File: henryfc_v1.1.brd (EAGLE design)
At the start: 36 x 36 mm, 69 parts, among them IC1 LM317DCYR, IC2 ICM-20602, IC3 AT7456E, IC4 STM32F722RET6TR, IC5 LM317DCYR, J2 10118192-0001LF, X1 SM07B-SRSS-TB, Y1 NX3225GA-27.000M-STD-CRG-1

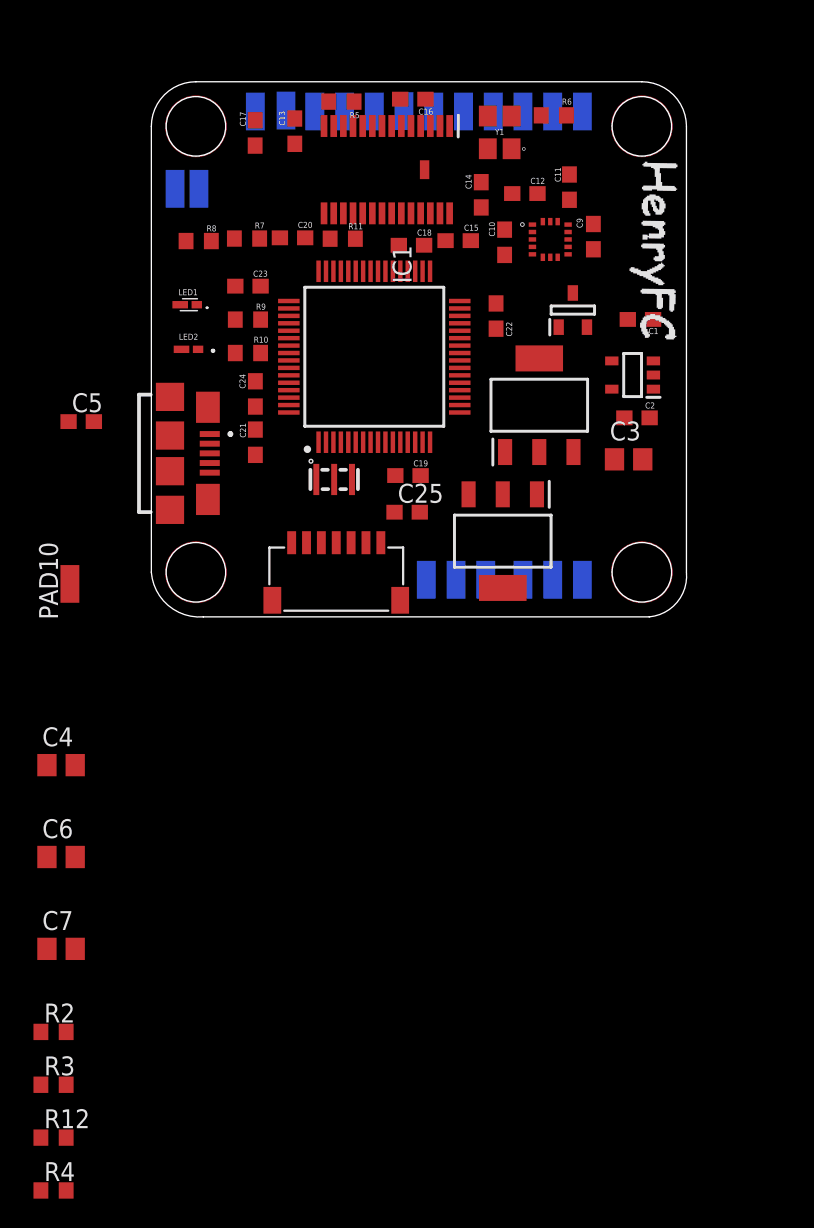
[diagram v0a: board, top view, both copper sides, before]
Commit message: edit bypass caps
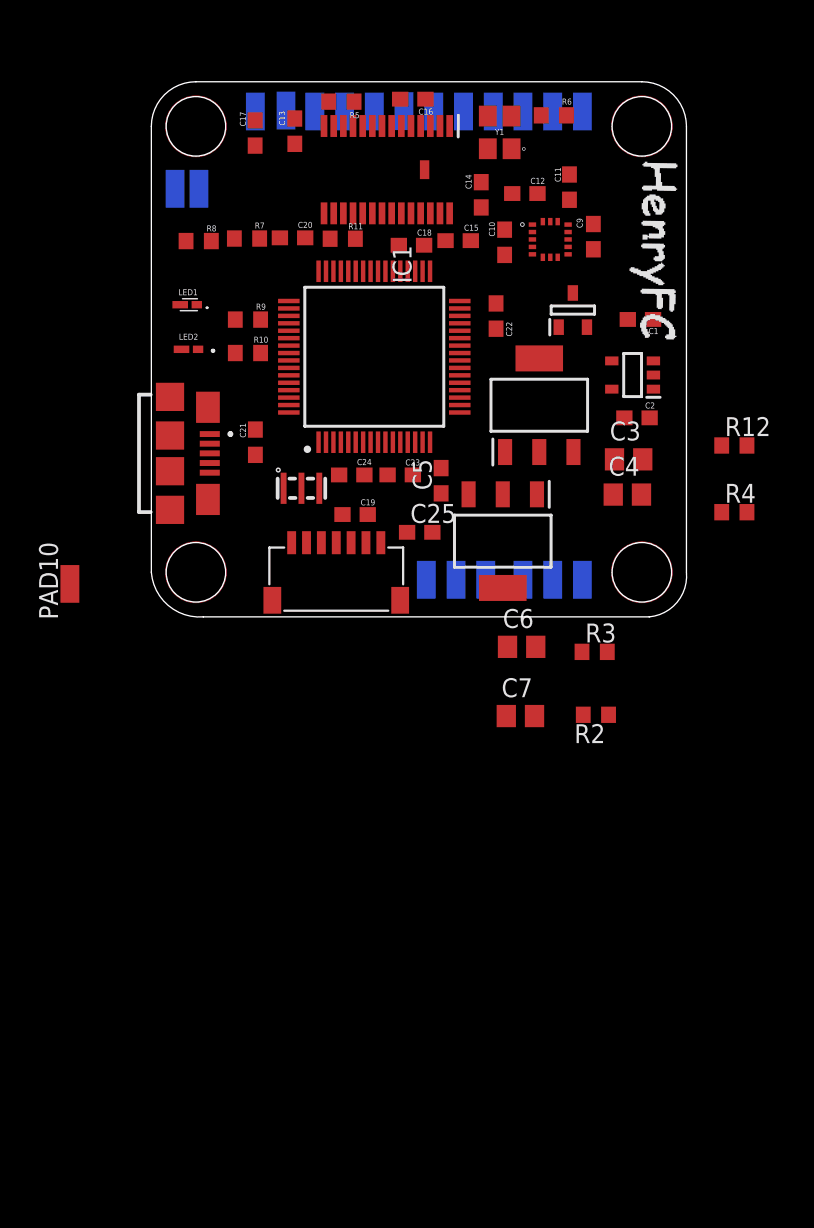
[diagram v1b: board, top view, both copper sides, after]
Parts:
- moved R12 65.3 mm to (40.7, 12.5)
- moved R4 64.7 mm to (40.7, 8.04)
- moved R3 46.6 mm to (31.3, -1.35)
- moved R2 42.3 mm to (31.4, -5.59), turned to 180 degrees
- moved C4 42.2 mm to (33.5, 9.23)
- moved C7 34.6 mm to (26.3, -5.67)
- moved C6 34.1 mm to (26.4, -1.02)
- moved C5 24.5 mm to (21.0, 10.2), turned to 90 degrees
- moved C23 16.3 mm to (18.2, 10.6)
- moved C24 8.47 mm to (15.0, 10.5), turned to 0 degrees
- moved C19 4.42 mm to (15.2, 7.88)
- moved R1 2.28 mm to (11.6, 9.65)
- moved C25 1.60 mm to (19.6, 6.69)

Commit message: update PCB layout
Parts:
- removed PAD10: BOOT, wirepad:SMD1,27-2,54
- added C26: 10uF, rcl:C0805
- added C8: 0.1uF, rcl:C0805
- moved R4 27.9 mm to (26.8, 32.2), turned to 90 degrees
- moved R12 22.6 mm to (29.5, 32.2)
- moved R6 21.7 mm to (7.73, 28.7), turned to 270 degrees
- moved R7 19.7 mm to (7.83, 6.71), turned to 270 degrees
- moved C21 18.6 mm to (24.2, 22.8), turned to 90 degrees
- moved C20 17.3 mm to (24.2, 15.4), turned to 270 degrees
- moved R8 16.8 mm to (8.34, 9.87), turned to 270 degrees
- moved Y1 15.4 mm to (9.53, 32.7)
- moved C19 14.8 mm to (24.2, 19.6), turned to 270 degrees
- moved C2 14.7 mm to (26.6, 27.0), turned to 180 degrees
- moved C11 14.5 mm to (30.1, 15.5), turned to 90 degrees
- moved C25 14.4 mm to (8.47, 15.9), turned to 90 degrees
- moved C10 14.1 mm to (27.5, 12.3), turned to 0 degrees
- moved R2 13.6 mm to (20.8, 2.88), turned to 0 degrees
- moved C7 13.5 mm to (23.0, 7.45), turned to 90 degrees
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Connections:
- net +5V: now also C26.2, C8.2; no longer PAD19.1, PAD20.1
- net 3.3V_REG: no longer PAD10.1
- net 5V_REG1: now also PAD19.1, PAD20.1
- net GND: now also C26.1, C8.1
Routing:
- net 3.3V_REG: track 0.00 -> 53.0 mm, vias 0 -> 1
- net 5V_REG1: track 0.00 -> 44.0 mm, vias 0 -> 1
- net VCC: track 0.00 -> 43.5 mm
- net 5V_USB: track 0.00 -> 34.0 mm, vias 0 -> 2
- net M3: track 0.00 -> 23.0 mm, vias 0 -> 2
- net +5V: track 0.00 -> 23.0 mm, vias 0 -> 1
- net M2: track 0.00 -> 23.0 mm, vias 0 -> 2
- net M1: track 0.00 -> 22.8 mm, vias 0 -> 2
- net M4: track 0.00 -> 22.8 mm, vias 0 -> 2
- net CURRENT_METER_ADC_PIN: track 0.00 -> 15.4 mm, vias 0 -> 2
- net VBAT_ADC_PIN: track 0.00 -> 14.5 mm
- net OSC_OUT: track 0.00 -> 11.7 mm
- net N$2: track 0.00 -> 11.6 mm
- net N$1: track 0.00 -> 11.1 mm
- net GYRO_1_CS_PIN: track 0.00 -> 10.5 mm
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
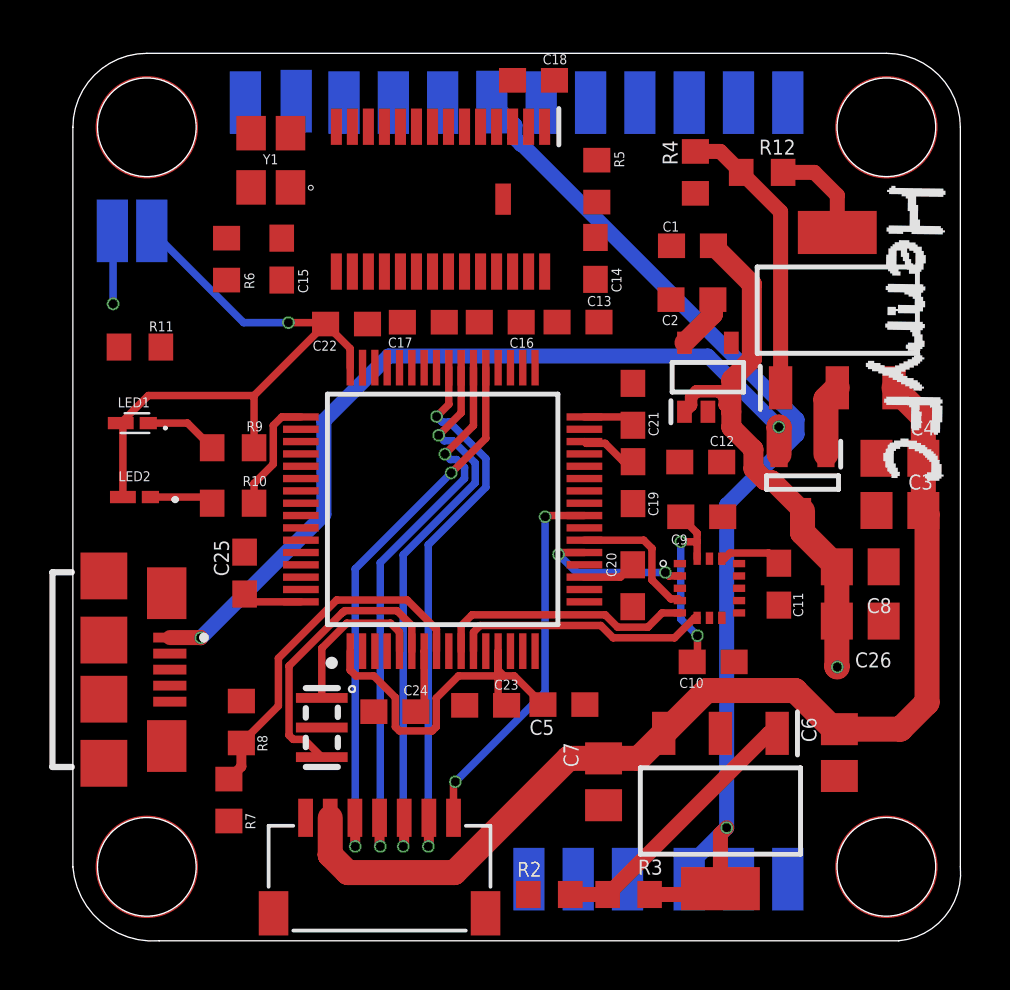
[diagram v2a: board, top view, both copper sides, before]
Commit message: update schematic
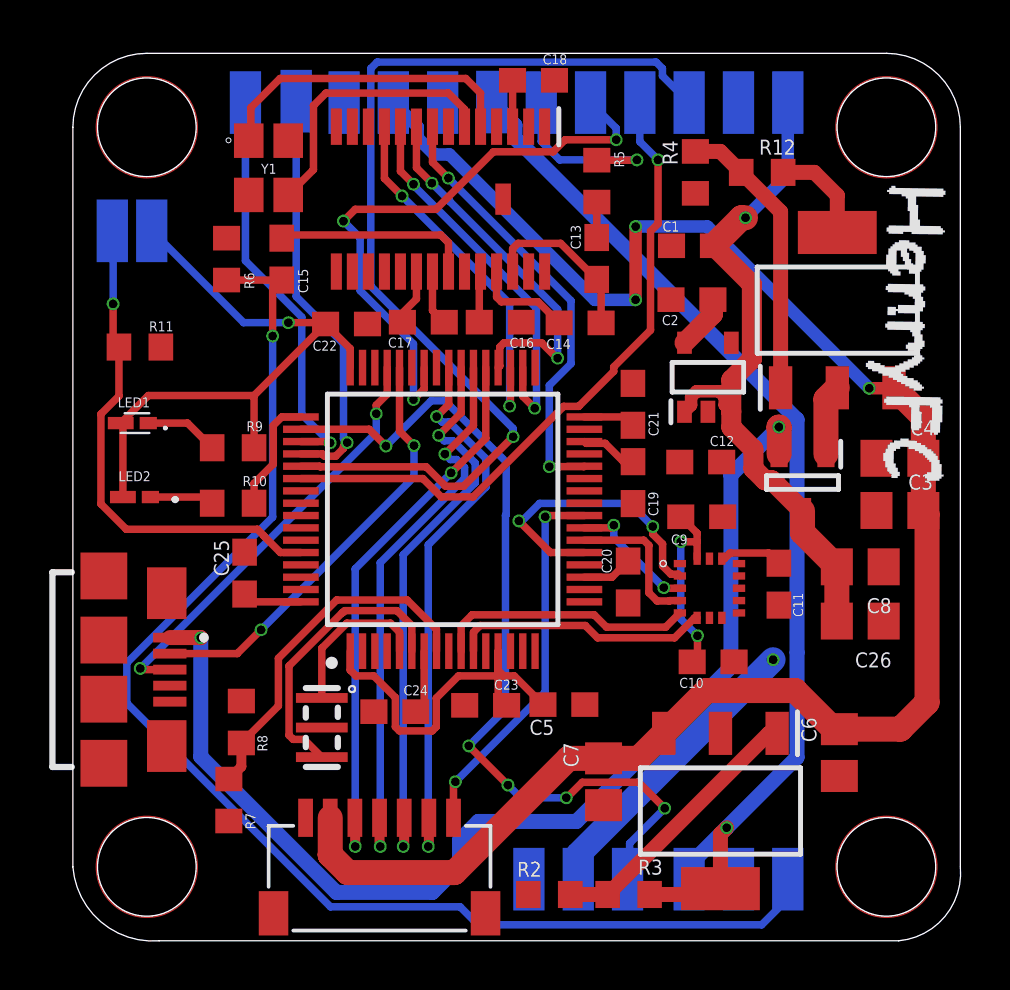
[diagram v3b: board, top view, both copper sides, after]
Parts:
- moved C13 2.69 mm to (22.7, 28.7), turned to 90 degrees
- moved C14 2.69 mm to (22.1, 26.1), turned to 0 degrees
- moved Y1 0.32 mm to (9.43, 32.4), turned to 270 degrees
- moved C20 0.24 mm to (24.0, 15.6)
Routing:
- net CAM_S: track 0.00 -> 53.8 mm, vias 0 -> 1
- net TX5: track 0.00 -> 41.0 mm, vias 0 -> 1
- net LED_STRIP: track 0.00 -> 36.1 mm, vias 0 -> 5
- net VCC: track 43.5 -> 73.1 mm, vias 0 -> 3
- net RX5: track 0.00 -> 27.1 mm, vias 0 -> 1
- net TX1: track 0.00 -> 24.3 mm, vias 0 -> 3
- net +5V: track 23.0 -> 46.7 mm, vias 1 -> 2
- net MAX7456_SPI_CS_PIN: track 0.00 -> 17.9 mm, vias 0 -> 2
- net OTG_FS_DP: track 0.00 -> 17.6 mm, vias 0 -> 2
- net OTG_FS_DM: track 0.00 -> 17.5 mm, vias 0 -> 2
- net BOOT: track 2.98 -> 20.4 mm
- net RX3: track 0.00 -> 16.9 mm, vias 0 -> 1
- net TX3: track 0.00 -> 16.4 mm, vias 0 -> 1
- net SPI2_SCK_PIN: track 0.00 -> 15.6 mm, vias 0 -> 2
- net SPI2_MOSI_PIN: track 0.00 -> 15.3 mm, vias 0 -> 2
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
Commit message: MORE SCHEMATIC REVISION
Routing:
- net 3.3V_REG: track 52.9 -> 108.1 mm, vias 1 -> 10
- net +5V: track 46.7 -> 77.1 mm, vias 2 -> 4
- net VCC: track 73.1 -> 77.7 mm
- net SPI2_MOSI_PIN: track 15.3 -> 18.6 mm
- net RX5: track 27.1 -> 27.7 mm
- net SPI2_MISO_PIN: track 15.0 -> 15.5 mm

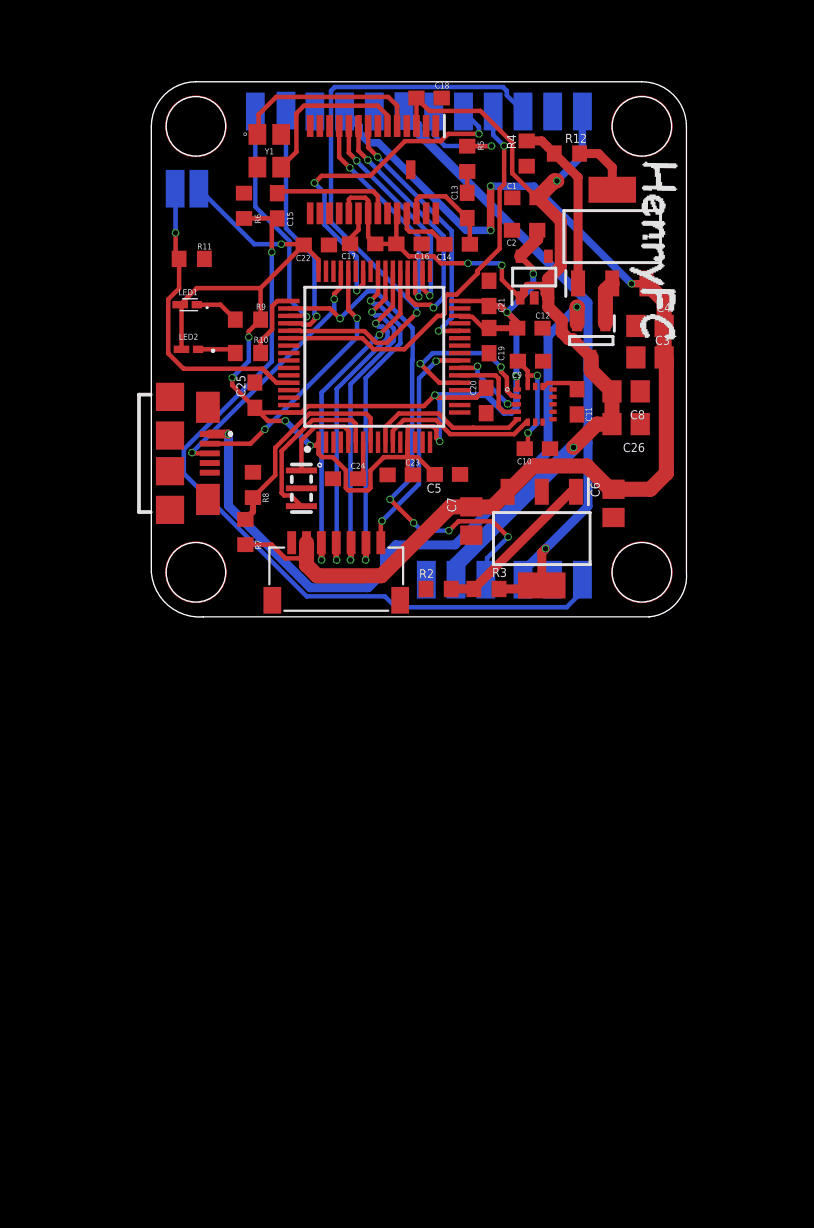
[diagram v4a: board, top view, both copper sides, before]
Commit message: finalized v1.2 PCB layout
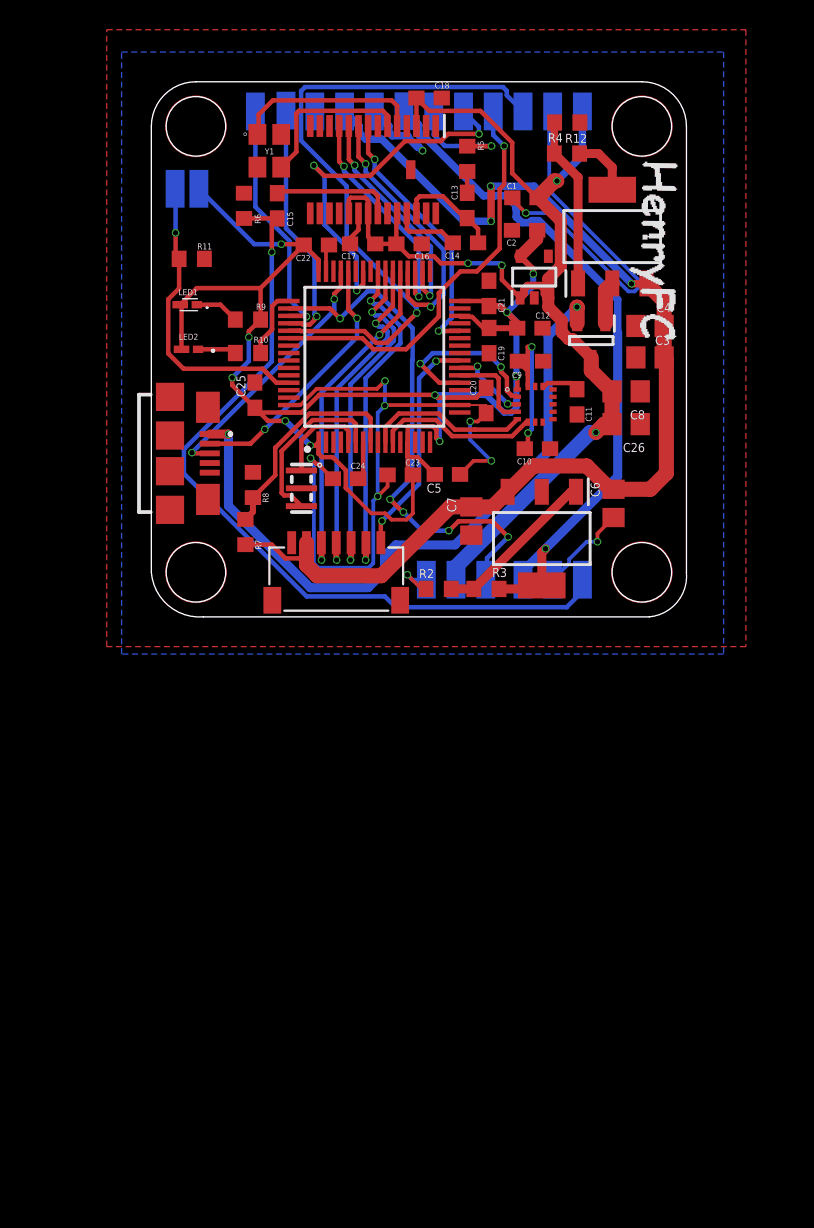
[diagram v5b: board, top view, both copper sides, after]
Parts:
- moved R4 3.43 mm to (29.5, 34.3), turned to 180 degrees
- moved C14 0.56 mm to (22.6, 26.2)
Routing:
- net GND: track 2.29 -> 93.3 mm, vias 0 -> 10
- net 5V_REG1: track 44.0 -> 47.6 mm
- net N$5: track 7.90 -> 10.9 mm
- net TX5: track 41.0 -> 43.8 mm
- net 3.3V_REG: track 108.1 -> 110.4 mm
- net TX1: track 24.3 -> 25.6 mm
- net VCC: track 77.7 -> 76.9 mm
- net N$8: track 4.01 -> 4.52 mm
- added copper zone on layer 1, net GND
- added copper zone on layer 16, net GND

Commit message: finalized PCB
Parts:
- PAD8: value LED_STRIP -> LED
